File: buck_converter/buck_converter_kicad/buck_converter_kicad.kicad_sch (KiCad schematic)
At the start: 24 parts, among them Q2 PMOS, Q3 NMOS, U1 ${SIM.PARAMS}, U4 ${SIM.PARAMS}, U5 ${SIM.PARAMS}

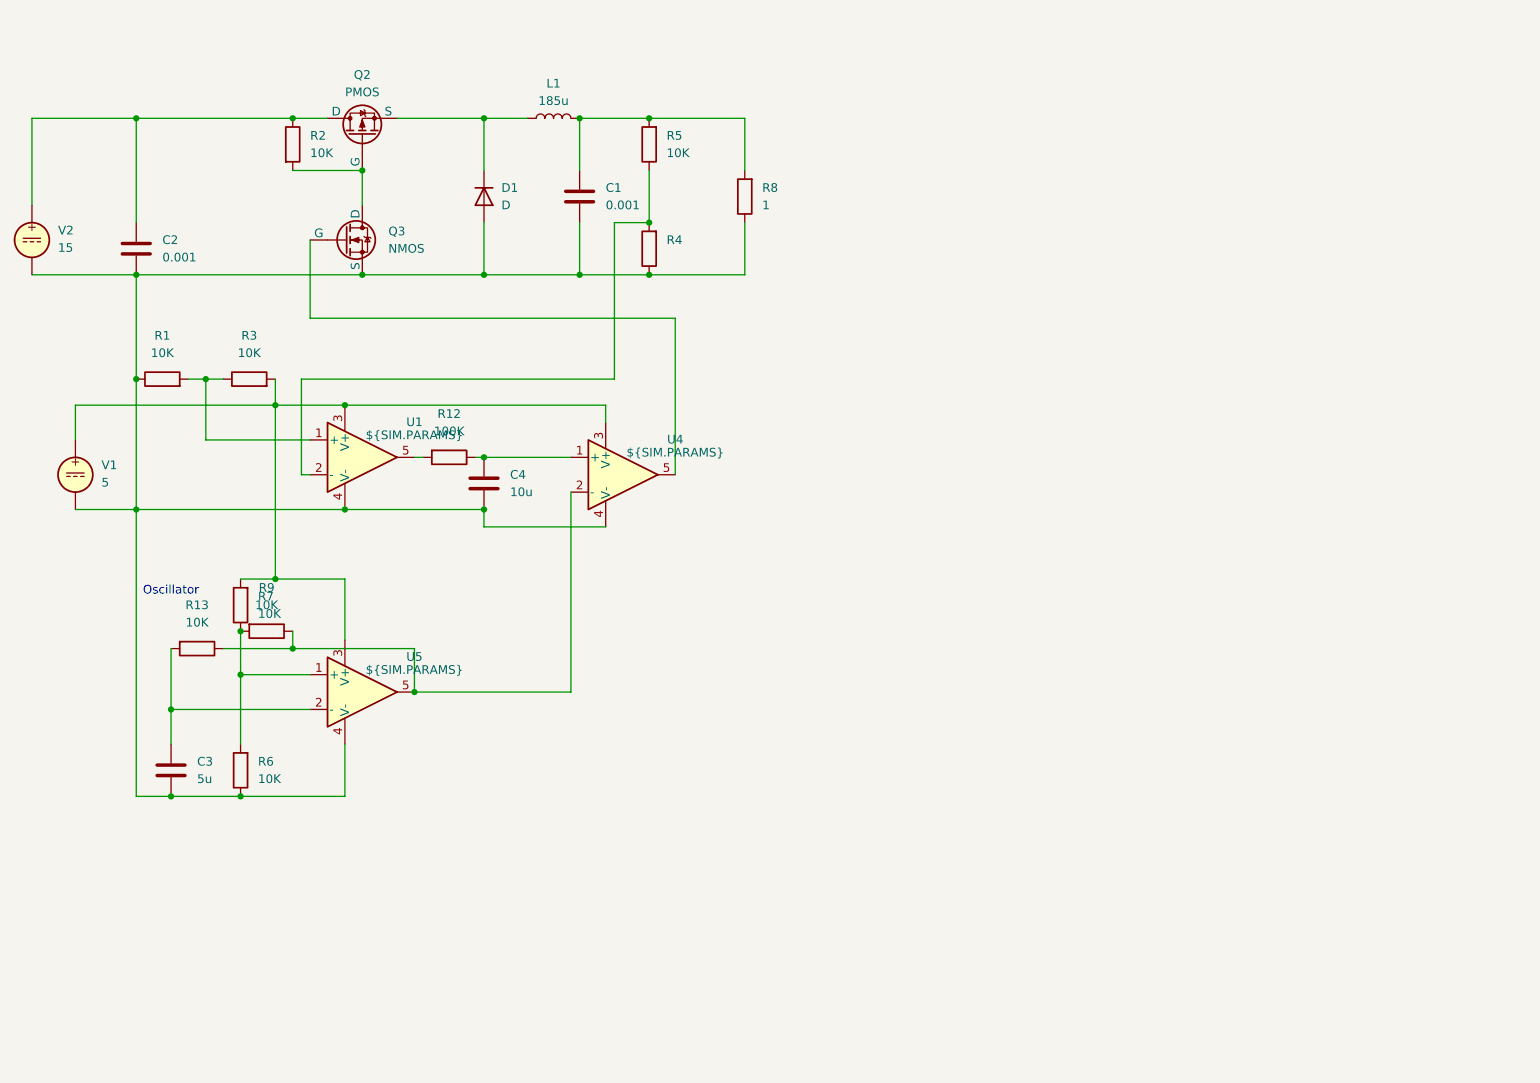
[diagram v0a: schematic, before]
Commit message: Buck converter
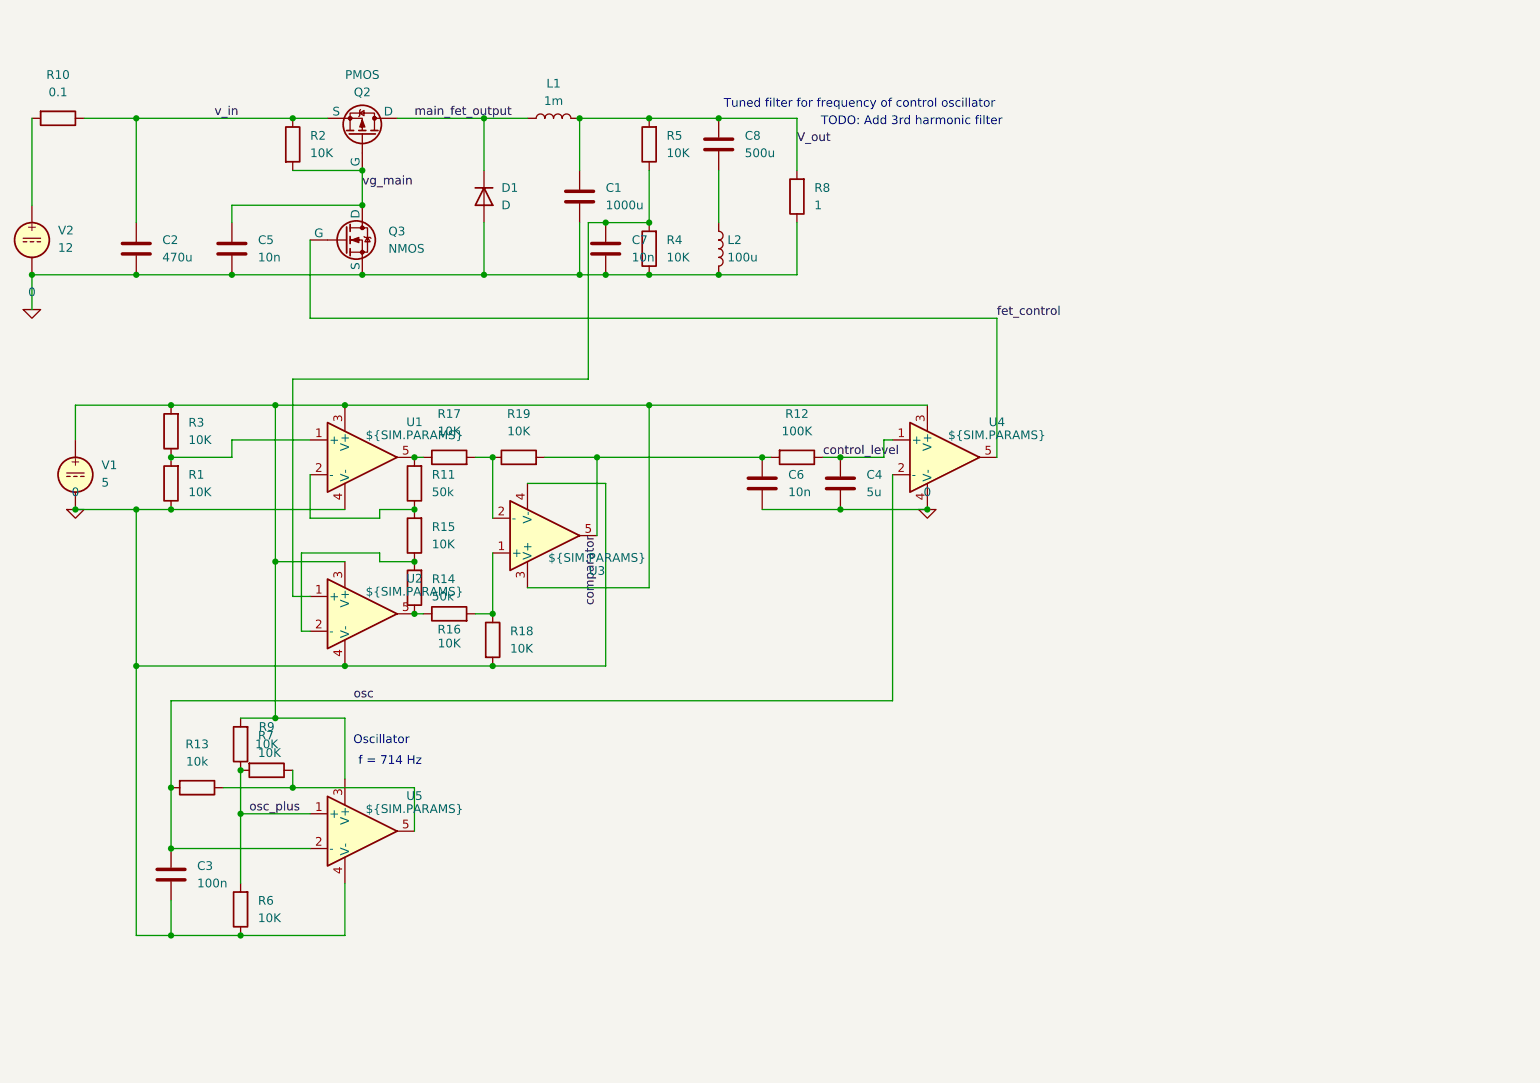
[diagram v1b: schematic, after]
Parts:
- added C5, C6, C7: 10n, symbol Device:C
- added C8: 500u, symbol Device:C
- added L2: 100u, symbol Device:L
- added R10: 0.1, symbol Device:R
- added R11, R14: 50k, symbol Device:R
- added R15, R16, R17, R18, R19: 10K, symbol Device:R
- added U2, U3: ${SIM.PARAMS}, symbol Simulation_SPICE:OPAMP
- C1: value 0.001 -> 1000u
- C2: value 0.001 -> 470u
- C3: value 5u -> 100n
- C4: value 10u -> 5u
- L1: value 185u -> 1m
- R13: value 10K -> 10k
- V2: value 15 -> 12
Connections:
- net v_in: now reaches C2.1, R2.1
- net v_in: now also Q2.3 (S), R10.1; no longer Q2.1 (D), V2.1
- net 0: now reaches C1.2, C2.2, C3.1, C4.1, D1.2 (A), Q3.3 (S), R1.1, R4.1, R6.1, R8.1, U1.4 (V-), U4.4 (V-), U5.4 (V-), V1.2, V2.2
- net 0: now also C5.2, C6.1, C7.1, L2.2, R18.2, U2.4 (V-), U3.4 (V-)
- net at R4.2, R5.1: now also C7.2, U2.1 (+); no longer U1.2 (-)
- net at R3.2, R7.2, U1.3 (V+)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: now also U2.3 (V+), U3.3 (V+)
- net at U1.5: now also R11.2, R17.1; no longer R12.2
- net osc_plus: now reaches R6.2, R7.1, R9.2, U5.1 (+)
- net control_level: now reaches C4.2, R12.1, U4.1 (+)
- net vg_main: now reaches Q2.2 (G), Q3.1 (D), R2.2
- net vg_main: now also C5.1
- net fet_control: now reaches Q3.2 (G), U4.5
- net main_fet_output: now reaches D1.1 (K), L1.1
- net main_fet_output: now also Q2.1 (D); no longer Q2.3 (S)
- net osc: now reaches C3.2, R13.2, U5.2 (-)
- net osc: now also U4.2 (-)
- net at R13.1, R9.1, U5.5: no longer U4.2 (-)
- net V_out: now reaches C1.1, L1.2, R5.2, R8.2
- net V_out: now also C8.1
- new net: R10.2, V2.1
- new net: R11.1, R15.2, U1.2 (-)
- new net: R14.2, R15.1, U2.2 (-)
- new net: R14.1, R16.1, U2.5
- new net: R16.2, R18.1, U3.1 (+)
- new net: C8.2, L2.1
- new net: R17.2, R19.1, U3.2 (-)
- new net comparator: C6.2, R12.2, R19.2, U3.5
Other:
- note added: "TODO: Add 3rd harmonic filter"
- note added: "Tuned filter for frequency of control oscillator"
- note added: "f = 714 Hz"
- moved on the sheet: C3, C4, Q2, R1, R12, R13, R3, R6, R7, R8, R9, U4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

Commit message: Buck converter
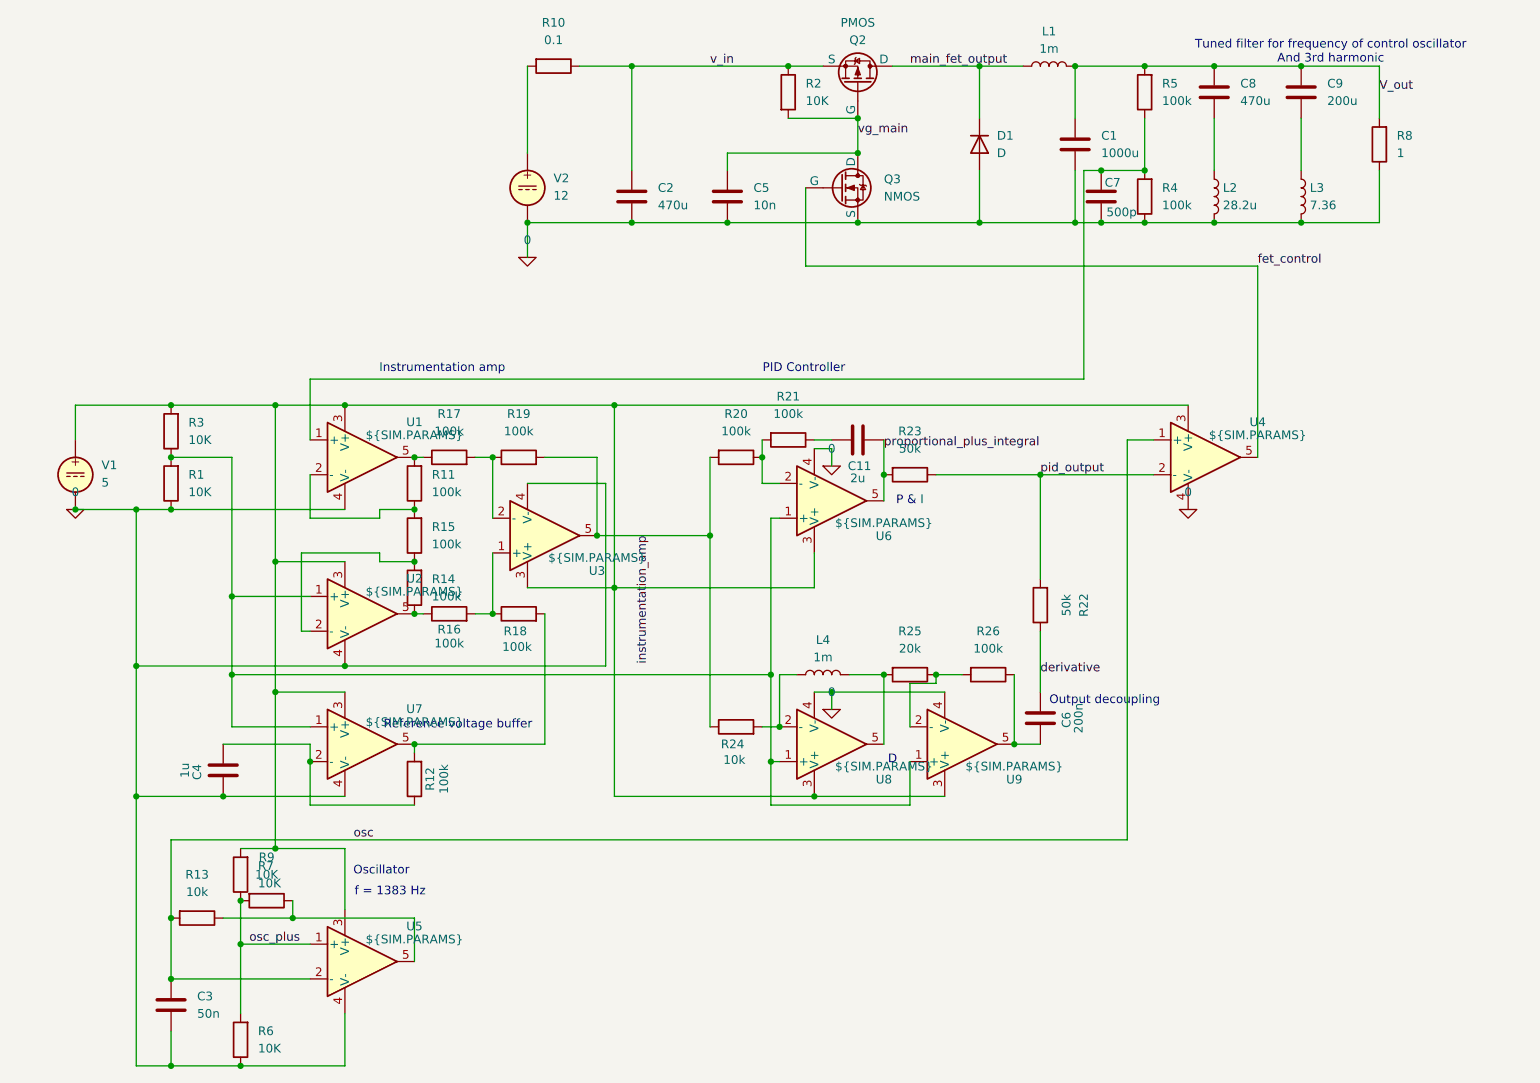
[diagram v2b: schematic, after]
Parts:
- added C11: 2u, symbol Device:C
- added C9: 200u, symbol Device:C
- added L3: 7.36, symbol Device:L
- added L4: 1m, symbol Device:L
- added R20, R21, R26: 100k, symbol Device:R
- added R22, R23: 50k, symbol Device:R
- added R24: 10k, symbol Device:R
- added R25: 20k, symbol Device:R
- added U6, U7, U8, U9: ${SIM.PARAMS}, symbol Simulation_SPICE:OPAMP
- C3: value 100n -> 50n
- C4: value 5u -> 1u
- C6: value 10n -> 200n
- C7: value 10n -> 500p
- C8: value 500u -> 470u
- L2: value 100u -> 28.2u
- R11, R14: value 50k -> 100k
- R12: value 100K -> 100k
- R15, R16, R17, R18, R19, R4, R5: value 10K -> 100k
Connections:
- net 0: now also C4.2, L3.2, U6.4 (V-), U7.4 (V-), U8.4 (V-), U9.4 (V-); no longer C4.1, C6.1, R18.2
- net V_out: now also C9.1
- net osc: now also U4.1 (+); no longer U4.2 (-)
- net at R1.2, R3.1: now also U2.1 (+), U6.1 (+), U7.1 (+), U8.1 (+), U9.1 (+); no longer U1.1 (+)
- net at R3.2, R7.2, U1.3 (V+)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: now also U6.3 (V+), U7.3 (V+), U8.3 (V+), U9.3 (V+)
- net at C7.2, R4.2, R5.1: now also U1.1 (+); no longer U2.1 (+)
- net comparator renamed instrumentation_amp
- net instrumentation_amp: now also R20.2, R24.1; no longer C6.2, R12.2
- removed net control_level: C4.2, R12.1, U4.1 (+)
- new net: C9.2, L3.1
- new net: C11.1, R21.1
- new net: R20.1, R21.2, U6.2 (-)
- new net: C4.1, R12.1, U7.2 (-)
- new net: R12.2, R18.2, U7.5
- new net: L4.1, R24.2, U8.2 (-)
- new net: L4.2, R25.2, U8.5
- new net: R25.1, R26.2, U9.2 (-)
- new net: C6.2, R26.1, U9.5
- new net derivative: C6.1, R22.1
- new net pid_output: R22.2, R23.1, U4.2 (-)
- new net proportional_plus_integral: C11.2, R23.2, U6.5
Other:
- note added: "D"
- note added: "Instrumentation amp"
- note added: "Output decoupling"
- note added: "P & I"
- note added: "PID Controller"
- note added: "Reference voltage buffer"
- note added: "Tuned filter for frequency of control oscillator And 3rd harmonic"
- note added: "f = 1383 Hz"
- note removed: "TODO: Add 3rd harmonic filter"
- note removed: "Tuned filter for frequency of control oscillator"
- note removed: "f = 714 Hz"
- moved on the sheet: C1, C2, C3, C5, C7, C8, D1, L1, L2, Q2, Q3, R10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

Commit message: Buck converter works well enough
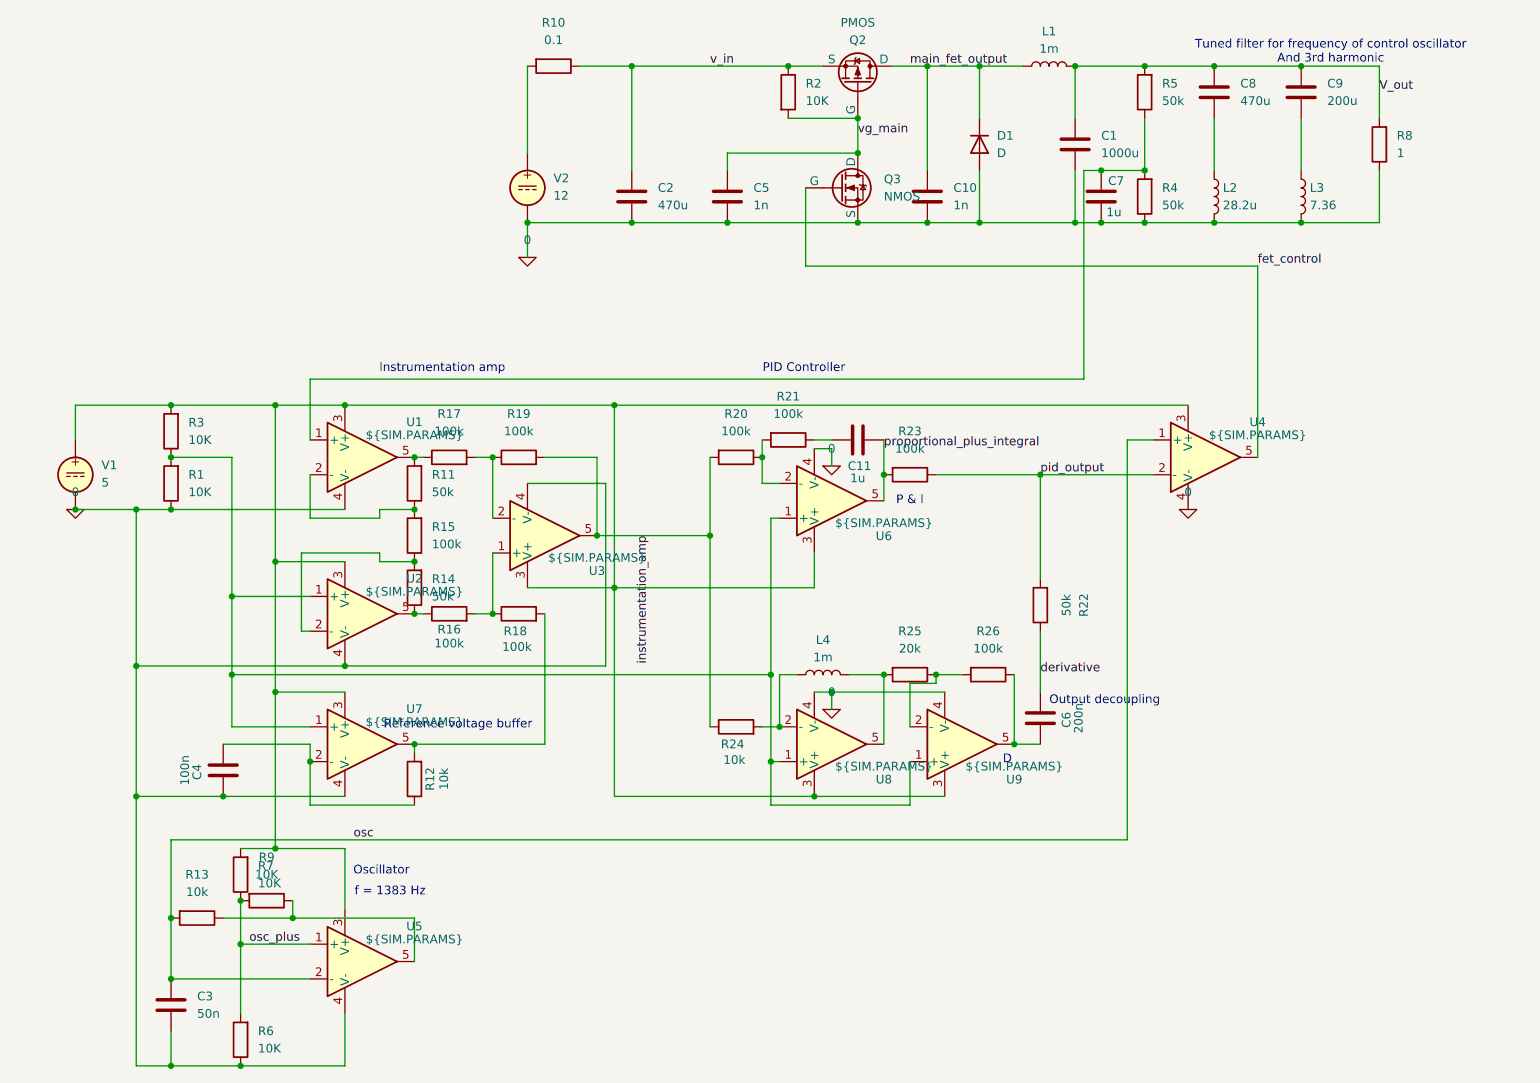
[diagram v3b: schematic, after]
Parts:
- added C10: 1n, symbol Device:C
- C11: value 2u -> 1u
- C4: value 1u -> 100n
- C5: value 10n -> 1n
- C7: value 500p -> 1u
- R11, R14, R4, R5: value 100k -> 50k
- R12: value 100k -> 10k
- R23: value 50k -> 100k
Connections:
- net 0: now also C7.2, C10.2; no longer C7.1
- net main_fet_output: now also C10.1
- net at R4.2, R5.1, U1.1 (+): now also C7.1; no longer C7.2

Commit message: xcvr work
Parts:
- C11: value 1u -> 3u
- C7: value 1u -> 200n
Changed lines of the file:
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@@
 			)
 		)
-		(property "Value" "1u"
+		(property "Value" "200n"
 			(at 191.262 63.246 0)
 			(effects
@@
 			)
 		)
-		(property "Value" "1u"
+		(property "Value" "3u"
 			(at 154.94 102.108 90)
 			(effects
